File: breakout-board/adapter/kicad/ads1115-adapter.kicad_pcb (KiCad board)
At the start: 2 copper layers, 42 x 19.7 mm, 7 parts, among them J1 TO BOARD J15, J2 TO BOARD J10, J3 ADS1115 10-PIN

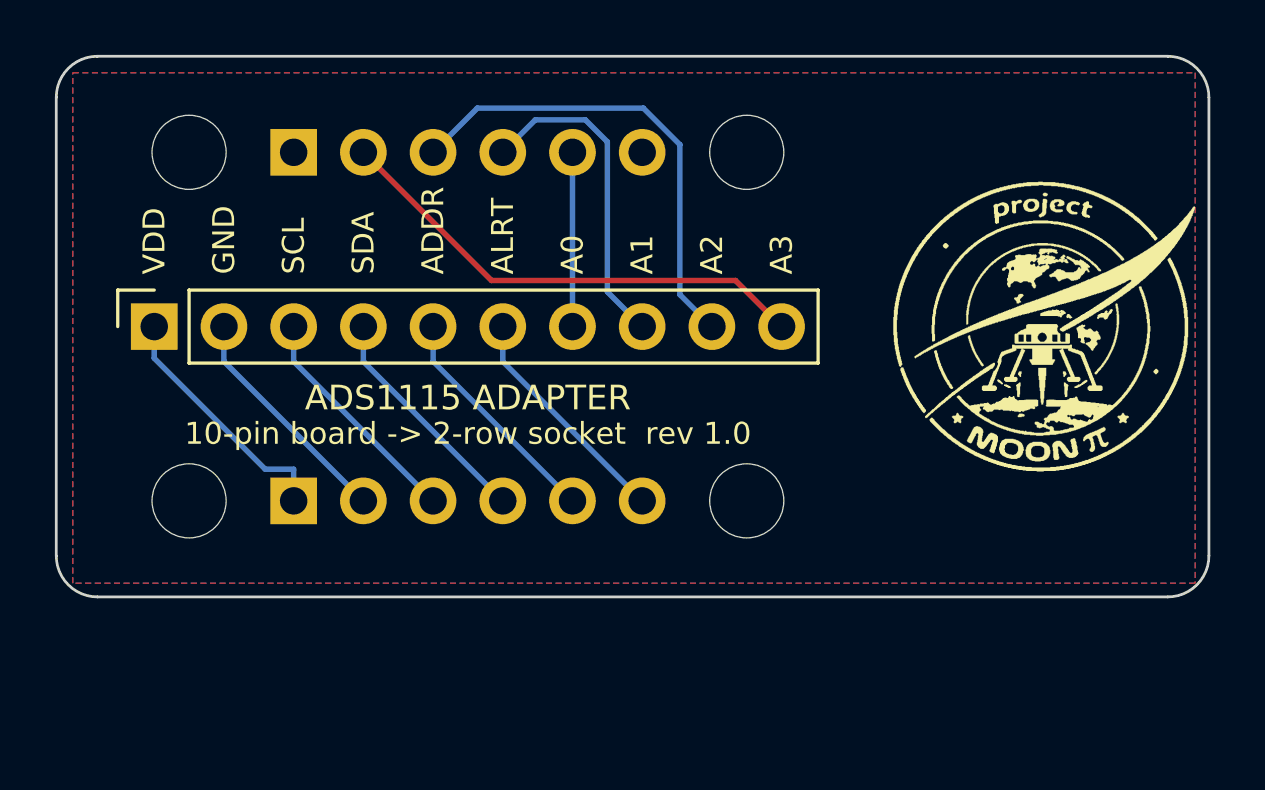
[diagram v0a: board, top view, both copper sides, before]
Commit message: Bigger logo on the breakout board; ADS1115 adapter rev 1.1 (module holes)
- Breakout board: Project Moon Pi logo 18 -> 26 mm in the top strip (silkscreen
  only, routing unchanged); Gerbers and pictures updated
- ADS1115 adapter rev 1.1: 5 mm taller (42 x 24.7 mm) with M2.5 holes H5/H6 for
  the 10-pin board's own mounting holes (original Adafruit layout), labelled on
  the silkscreen; README fitting order and parts list updated

Co-Authored-By: Claude Opus 5.5 <noreply@anthropic.com>
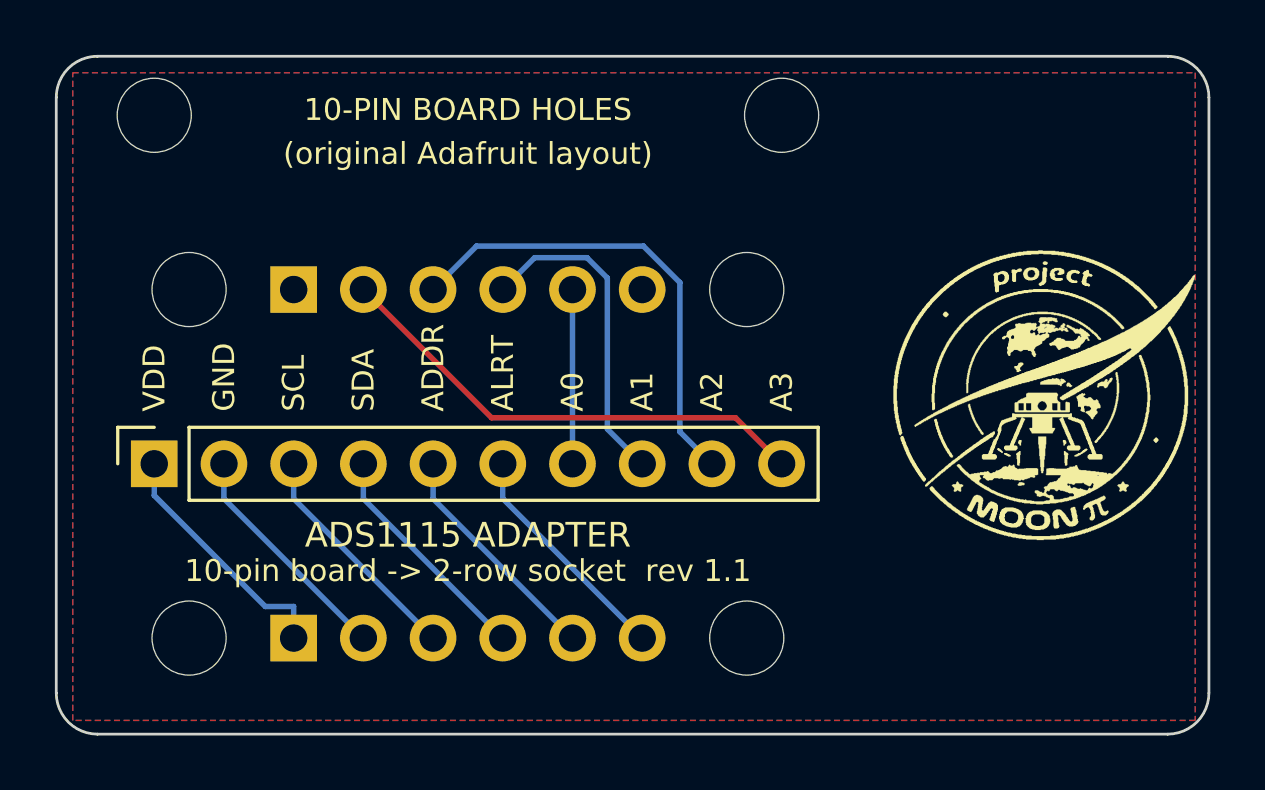
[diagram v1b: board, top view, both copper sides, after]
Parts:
- added H5: M2.5, MountingHole:MountingHole_2.7mm_M2.5, F.Cu at (3.57, 2.15)
- added H6: M2.5, MountingHole:MountingHole_2.7mm_M2.5, F.Cu at (26.4, 2.15)
- moved H1 5.00 mm to (4.84, 8.50)
- moved H2 5.00 mm to (25.2, 8.50)
- moved H3 5.00 mm to (4.84, 21.2)
- moved H4 5.00 mm to (25.2, 21.2)
- moved J1 5.00 mm to (8.65, 8.50)
- moved J2 5.00 mm to (8.65, 21.2)
- moved J3 5.00 mm to (3.57, 14.8)
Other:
- board size 42 x 19.7 mm -> 42 x 24.7 mm
- board text added: "(original Adafruit layout)"
- board text added: "10-PIN BOARD HOLES"
- board text added: "10-pin board -> 2-row socket rev 1.1"
- board text removed: "10-pin board -> 2-row socket rev 1.0"

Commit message: Board rev 2.8 re-layout: ribbon header on the top edge, amps side by side, 9 mounting holes, standoff keepouts
- Pi ribbon header J1 and the power LEDs move to the top edge (ribbon goes
  straight up to the lid); TILT plug to the top-left corner
- Stereo amp site J16 now sits beside the mono amp J9 ("fit one amp only")
- 9 M3 mounting holes against vibration: corners, mid-sides (H15-H18) and
  one near the centre (H19); drilling template updated
- Copper-free rings around every hole on both sides (M3 r 4 mm, M2.5 r 3 mm,
  extended to nearby edges): brass standoffs need no insulating washers and
  never tie board ground to the box
- ADS1115 adapter: same standoff keepouts
- README, parts list and BOM spreadsheet updated (9 M3 standoffs, brass notes)

Co-Authored-By: Claude Opus 5.5 <noreply@anthropic.com>
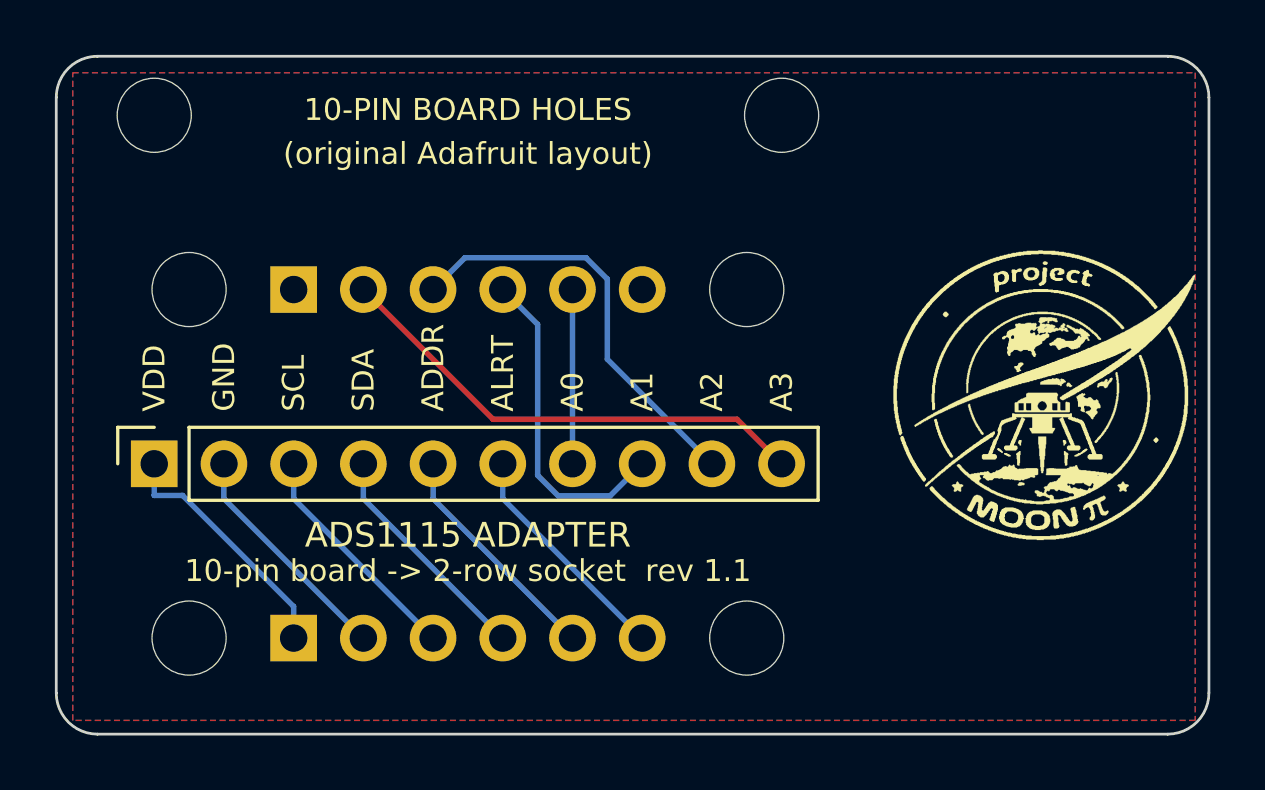
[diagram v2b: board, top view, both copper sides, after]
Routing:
- net /A2: track 17.3 -> 15.5 mm
